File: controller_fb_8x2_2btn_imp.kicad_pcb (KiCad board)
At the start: 2 copper layers, 105 x 35.9 mm, 19 parts, among them J1 Conn_01x19, SW1 SW_Push_LED, SW2 SW_Push_LED, SW3 Rotary_Encoder_with_Dual_LED_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

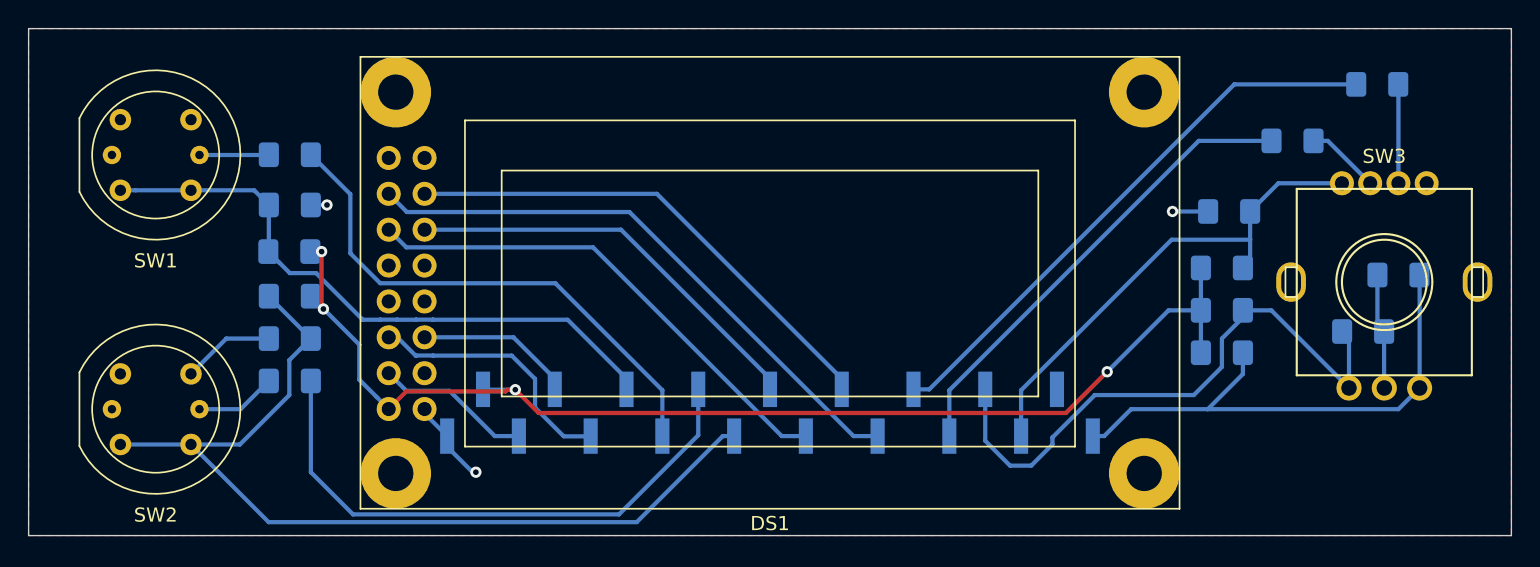
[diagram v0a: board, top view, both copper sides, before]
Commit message: Init v0.2
    - Unifying a button connections
    - Enlarge button holes
    - Decrease PCB high -0.2mm x 2
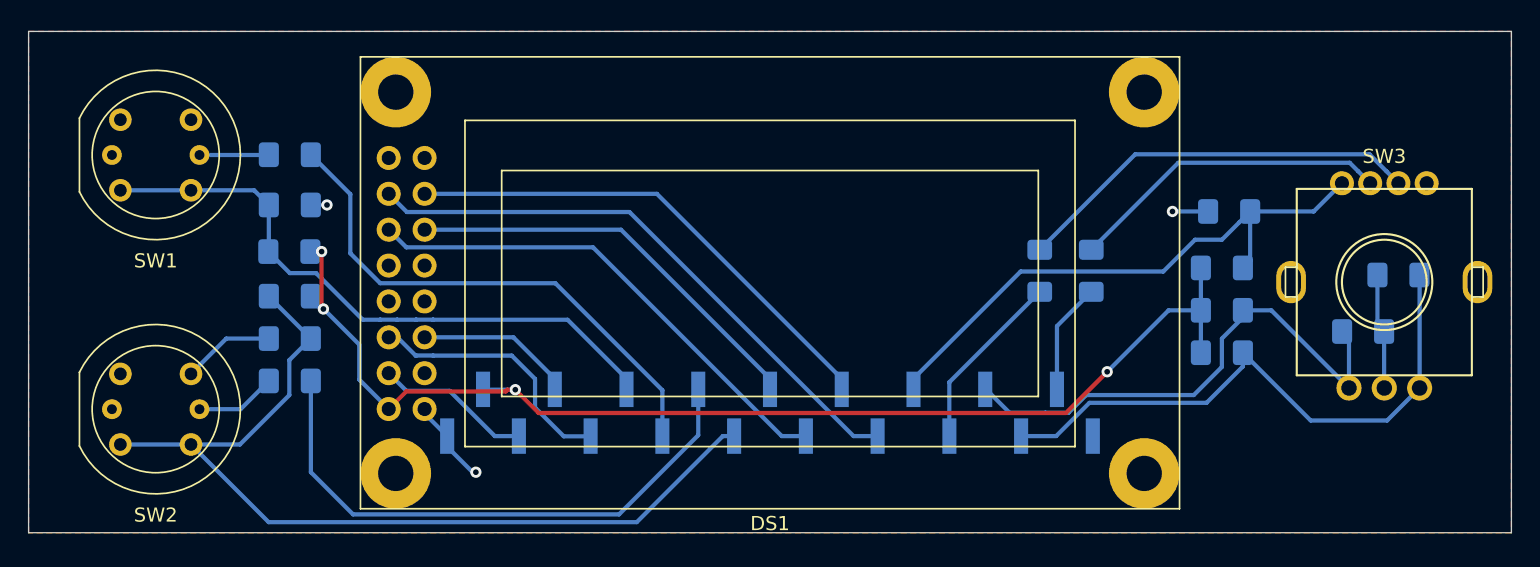
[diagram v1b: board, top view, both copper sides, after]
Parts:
- moved R7 27.3 mm to (181.6, 101.2), turned to 90 degrees
- moved R8 17.0 mm to (185.2, 101.2), turned to 90 degrees
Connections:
- C4 pad 1: /PC0(INT3) -> /PB6
- C5 pad 1: /PB6 -> /PB3
- J1 pad 18: (no net) -> /PD0
- J1 pad 19: /PC0(INT3) -> (no net)
- R5 pad 2: /PC0(INT3) -> /PB6
- R7 pad 1: /PB3 -> /PB4
- R8 pad 1: /PB4 -> /PD0
- R9 pad 2: /PB6 -> /PB3
- SW3 pad 4: /PB6 -> /PB3
- SW3 pad B: /PC0(INT3) -> /PB6
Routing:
- net /PC0(INT3): track 37.6 -> 0.00 mm
- net Net-(R7-Pad2): track 7.01 -> 29.1 mm
- net /PB4: track 33.4 -> 12.9 mm
- net Net-(R8-Pad2): track 5.26 -> 22.9 mm
- net /PD0: track 0.00 -> 7.91 mm
- net /PB6: track 35.4 -> 42.2 mm
- net /PB5(INT2): track 42.9 -> 37.5 mm
- net /PB3: track 40.3 -> 41.0 mm
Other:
- board size 105 x 35.9 mm -> 105 x 35.5 mm
